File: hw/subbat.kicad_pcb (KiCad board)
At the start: 2 copper layers, 100 x 100 mm, 165 parts, among them J1 Conn_01x02_Female, J10 USB_Ax2, J11 Conn_01x02_Female, J2 Barrel_Jack, J3 USB_Ax2, J4 USB_Ax2, J5 Conn_01x02_Female, J6 Conn_WallSocket, J7 USB_B_Micro, J8 USB_Ax2, J9 USB_Ax2, K1 953-1C-5DG-1, P1 Conn_WallPlug, P2 CONN_01X06, P3 CONN_01X06, P4 CONN_01X06, Q1 DMP3007SCG, Q2 2N7002, Q3 2N7002, Q4 Q_PMOS_GSD, Q5 BTA24-600CW, Q6 Q_NPN_BEC, Q7 Q_NPN_BEC, SW1 SW_SPDT_WITH_SHIELD, SW2 SW_SPDT_WITH_SHIELD, SW3 SW_PUSH_SMALL_H, SW4 SW_PUSH_SMALL_H, U1 PC817, U2 TPS53319, U3 CM1293A-04SO, U4 AZ1117-3.3, U5 AZ1117-5.0, U6 CH340G, U7 CM1293A-04SO, U8 ESP-WROOM-02, U9 TLP561J, Y1 Crystal

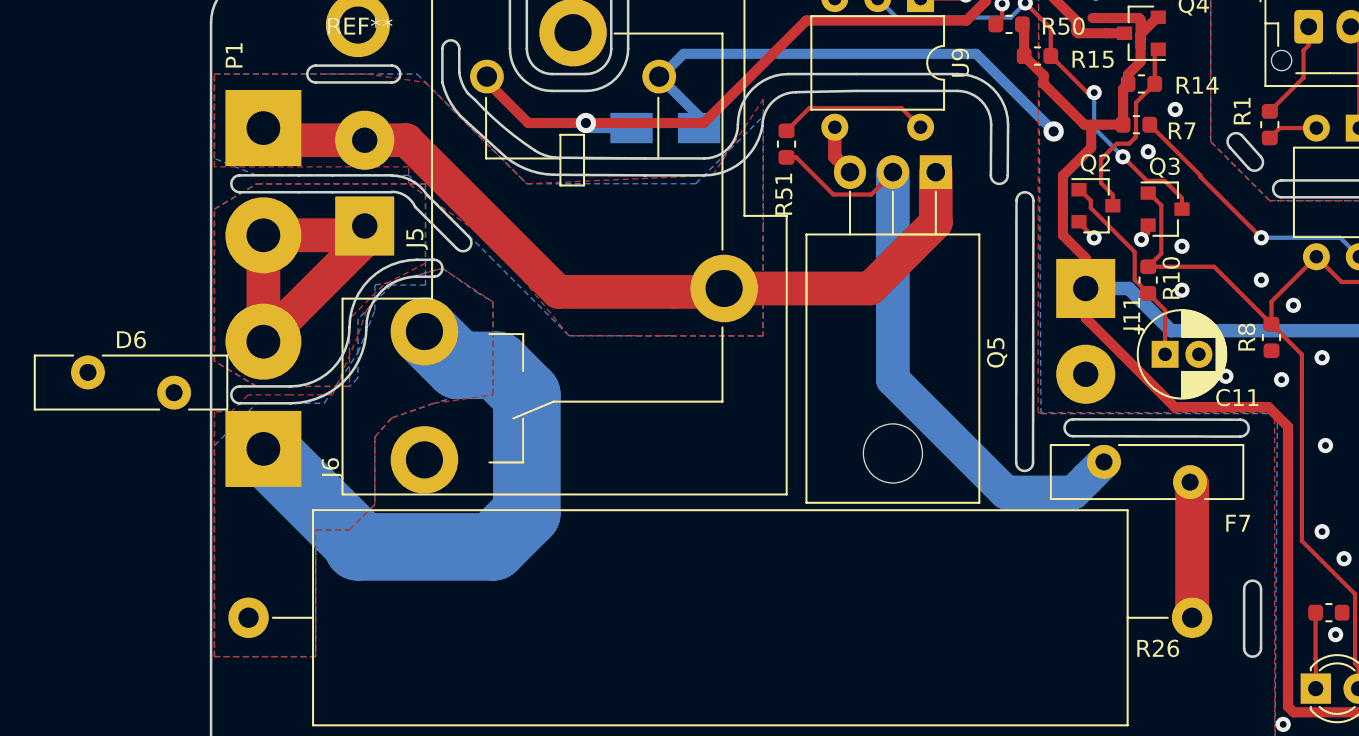
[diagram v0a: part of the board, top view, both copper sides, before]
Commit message: Added a spark killer
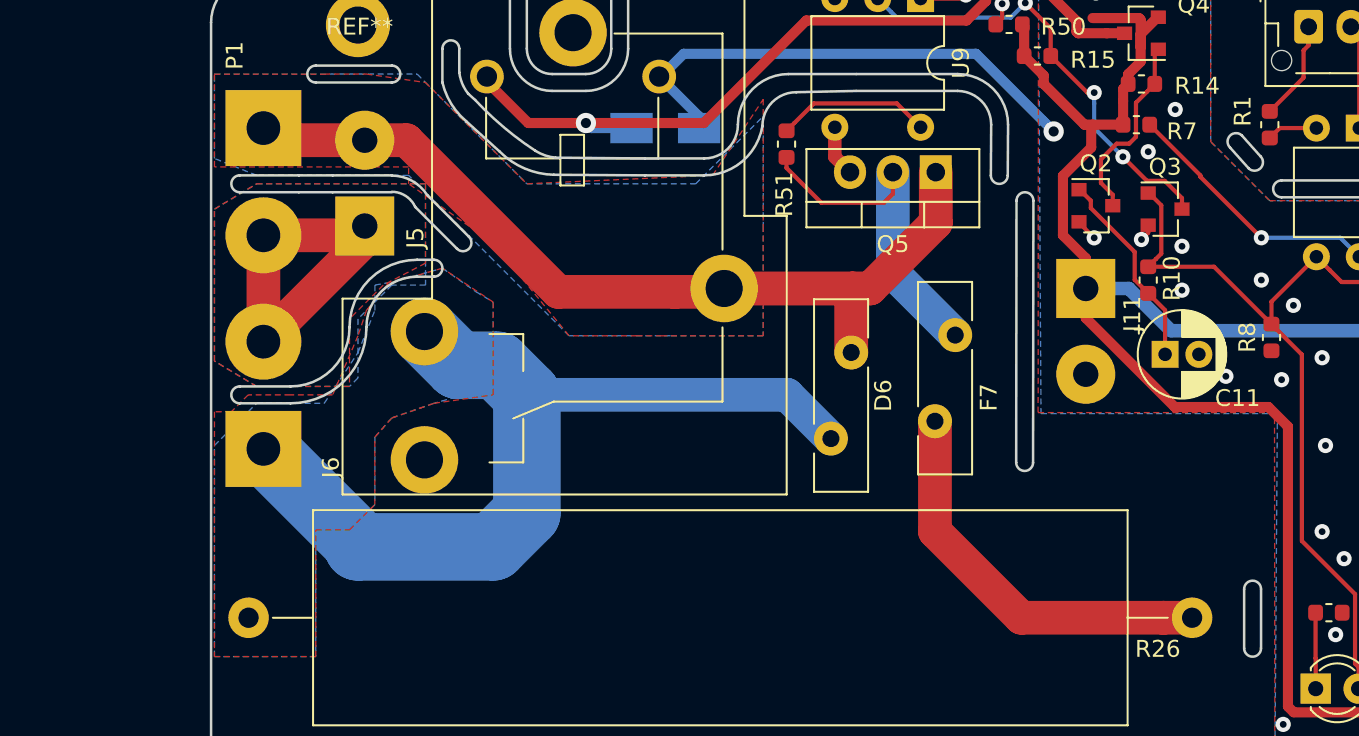
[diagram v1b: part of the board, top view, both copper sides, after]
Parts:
- Q5: footprint Package_TO_SOT_THT:TO-220-3_Horizontal_TabDown -> Package_TO_SOT_THT:TO-220-3_Vertical
- moved D6 45.2 mm to (57.9, 42.3), turned to 270 degrees
- moved F7 15.5 mm to (62.9, 46.4), turned to 90 degrees
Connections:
- J7 pad 4: (no net) -> Net-(J7-Pad4)
- K1 pad 2: (no net) -> Net-(K1-Pad2)
- P2 pad 1: (no net) -> Net-(P2-Pad1)
- P4 pad 1: (no net) -> Net-(P4-Pad1)
- SW1 pad 3: (no net) -> Net-(SW1-Pad3)
- SW2 pad 1: (no net) -> Net-(SW2-Pad1)
- U2 pad 22: (no net) -> Net-(U2-Pad22)
- U6 pad 10: (no net) -> Net-(U6-Pad10)
- U6 pad 11: (no net) -> Net-(U6-Pad11)
- U6 pad 12: (no net) -> Net-(U6-Pad12)
- U6 pad 15: (no net) -> Net-(U6-Pad15)
- U6 pad 9: (no net) -> Net-(U6-Pad9)
- U8 pad 10: (no net) -> Net-(U8-Pad10)
- U8 pad 14: (no net) -> Net-(U8-Pad14)
- U8 pad 16: (no net) -> Net-(U8-Pad16)
- U8 pad 17: (no net) -> Net-(U8-Pad17)
- U8 pad 3: (no net) -> Net-(U8-Pad3)
- U8 pad 4: (no net) -> Net-(U8-Pad4)
- U9 pad 3: (no net) -> Net-(U9-Pad3)
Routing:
- net /AC_OUT_L: track 33.6 -> 52.6 mm
- net Net-(F7-Pad1): track 8.08 -> 23.9 mm
- net Net-(F7-Pad2): track 36.1 -> 20.5 mm
- net /AC_IN_L: track 48.3 -> 52.2 mm
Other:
- outline, holes or cut-outs redrawn

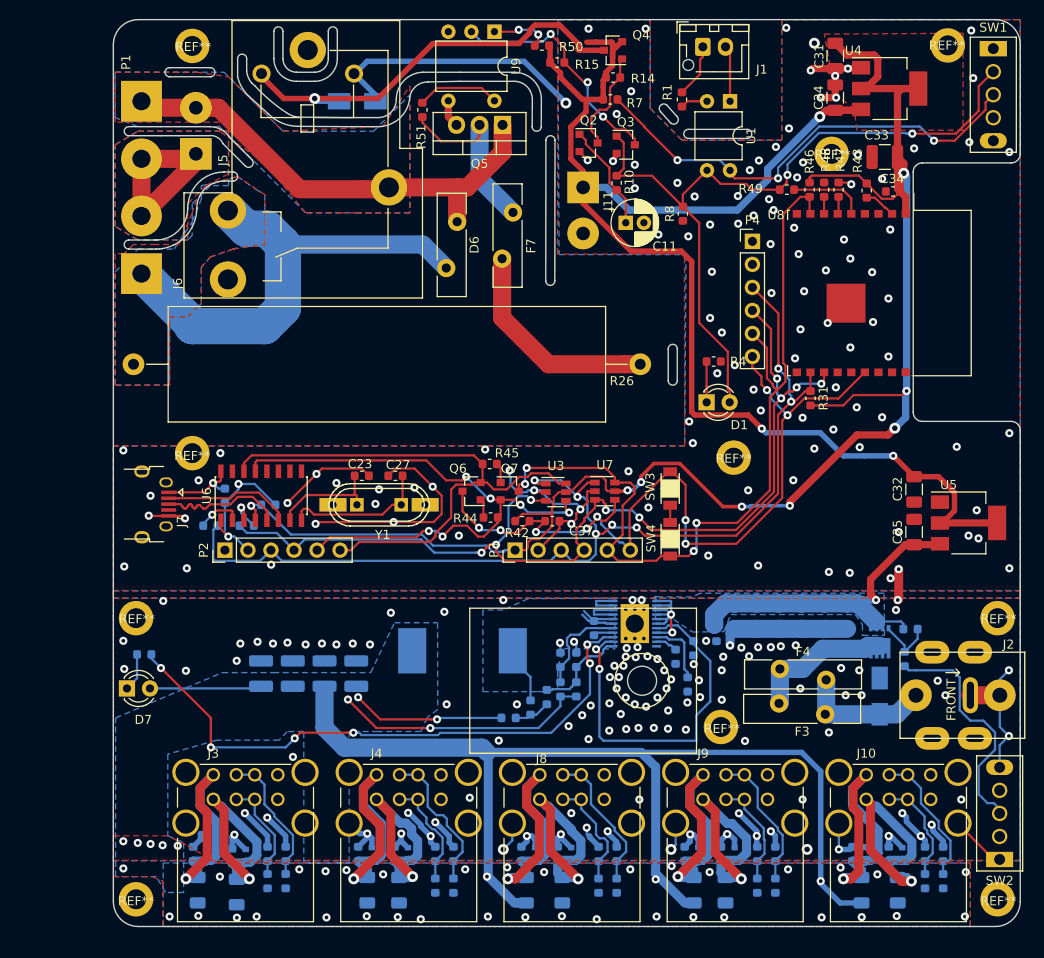
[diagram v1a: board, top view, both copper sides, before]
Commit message: To make easy chassis making
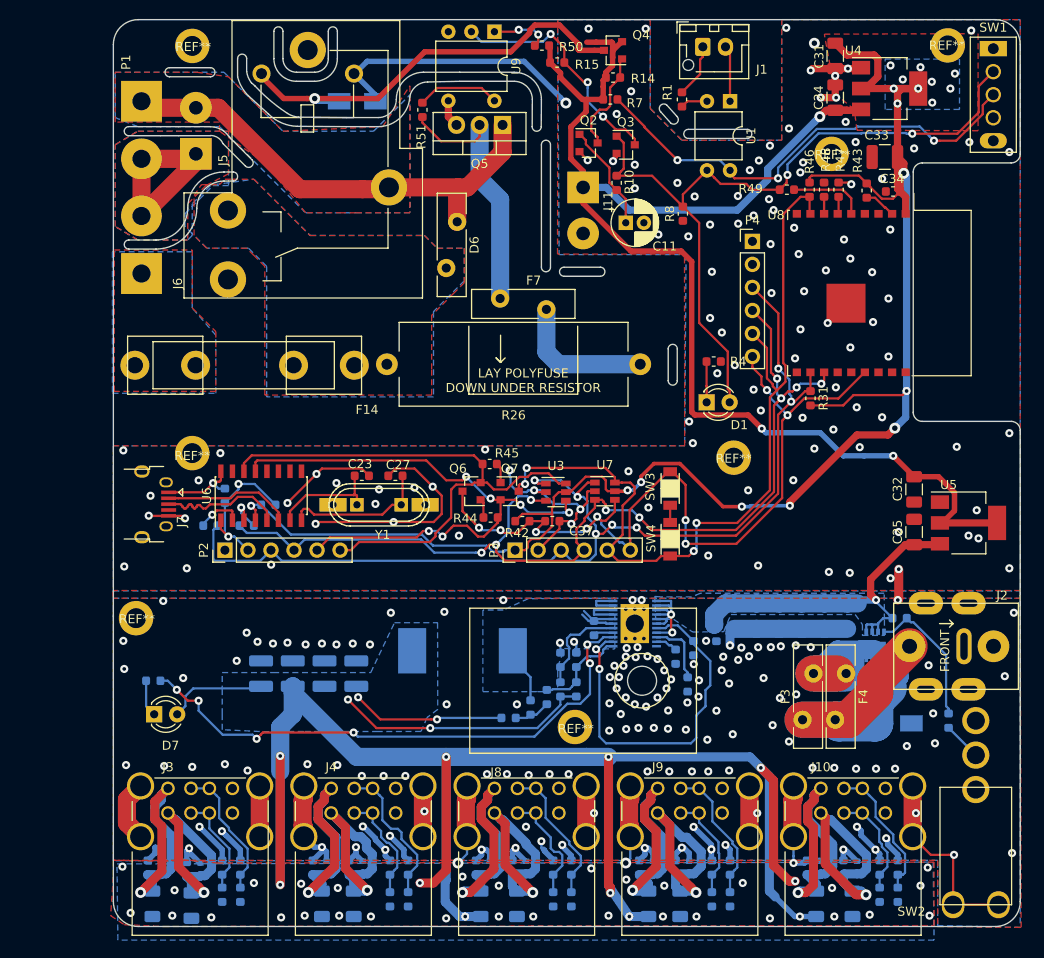
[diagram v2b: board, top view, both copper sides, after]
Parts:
- removed the REF** at (117.5, 117.0)
- removed the REF** at (117.5, 86.0)
- removed the REF** at (22.5, 117.0)
- added F14: 15A, components:FUSE-HOLDER-FUC-03A-20mm_x_5.2mm, F.Cu at (46.6, 58.1)
- F3, F4: footprint Fuse:Fuse_Bourns_MF-RG800 -> Fuse:Fuse_Bourns_MF-RG700
- R26: footprint Resistor_THT:R_Axial_Power_L48.0mm_W12.5mm_P55.88mm -> Resistor_THT:R_Axial_Power_L25.0mm_W9.0mm_P27.94mm
- SW2: footprint components:SW_SPDT_WITH_SHILD -> components:SW_SPDT_v
- moved REF** 16.1 mm to (70.9, 98.0)
- moved R12 8.35 mm to (112.1, 97.3)
- moved F7 7.42 mm to (67.8, 52.0), turned to 180 degrees
- moved F4 7.32 mm to (100.8, 92.1), turned to 270 degrees
- moved SW2 5.64 mm to (115.1, 117.6)
- moved J2 5.45 mm to (119.8, 89.1)
- moved C10 5.22 mm to (28.1, 113.7)
- moved C15 5.22 mm to (42.0, 113.5)
- moved C16 5.22 mm to (46.0, 113.5)
- moved C21 5.22 mm to (60.0, 113.5)
- moved C22 5.22 mm to (64.0, 113.5)
- moved C29 5.22 mm to (78.0, 113.5)
- moved C30 5.22 mm to (82.0, 113.5)
- moved C35 5.22 mm to (96.5, 113.5)
- moved C36 5.22 mm to (100.5, 113.5)
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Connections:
- J6 pad 1: /AC_OUT_L -> /AC_OUT_L_2
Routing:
- net VCOM: track 174.8 -> 258.1 mm, vias 47 -> 46
- net /AC_OUT_L: track 52.6 -> 0.00 mm
- net GND: track 249.6 -> 301.7 mm, vias 237 -> 260
- net Net-(D2-Pad1): track 14.7 -> 45.7 mm
- net Net-(R12-Pad1): track 25.6 -> 4.26 mm
- net Net-(Q1-Pad4): track 6.46 -> 15.7 mm
- net Net-(F7-Pad2): track 20.5 -> 29.4 mm
- net Net-(F7-Pad1): track 23.9 -> 15.6 mm
- net Net-(R25-Pad2): track 66.2 -> 61.8 mm
- net Net-(F3-Pad2): track 15.9 -> 19.0 mm
- net /VIN: track 58.7 -> 55.9 mm
- net +3V3: vias 8 -> 18
- net (no net): vias 0 -> 1
- added copper zone on B.Cu, net +3V3
- added copper zone on B.Cu, net /AC_OUT_L_2
- added copper zone on F.Cu, net /AC_OUT_L_2
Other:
- outline, holes or cut-outs redrawn
- board text added: "LAY POLYFUSE DOWN UNDER RESISTOR"
